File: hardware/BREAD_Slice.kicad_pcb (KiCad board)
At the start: 2 copper layers, 70 x 100 mm, 22 parts, among them J1 Conn_01x10_Socket, SW1 SW_DIP_x04, U1 AP63205

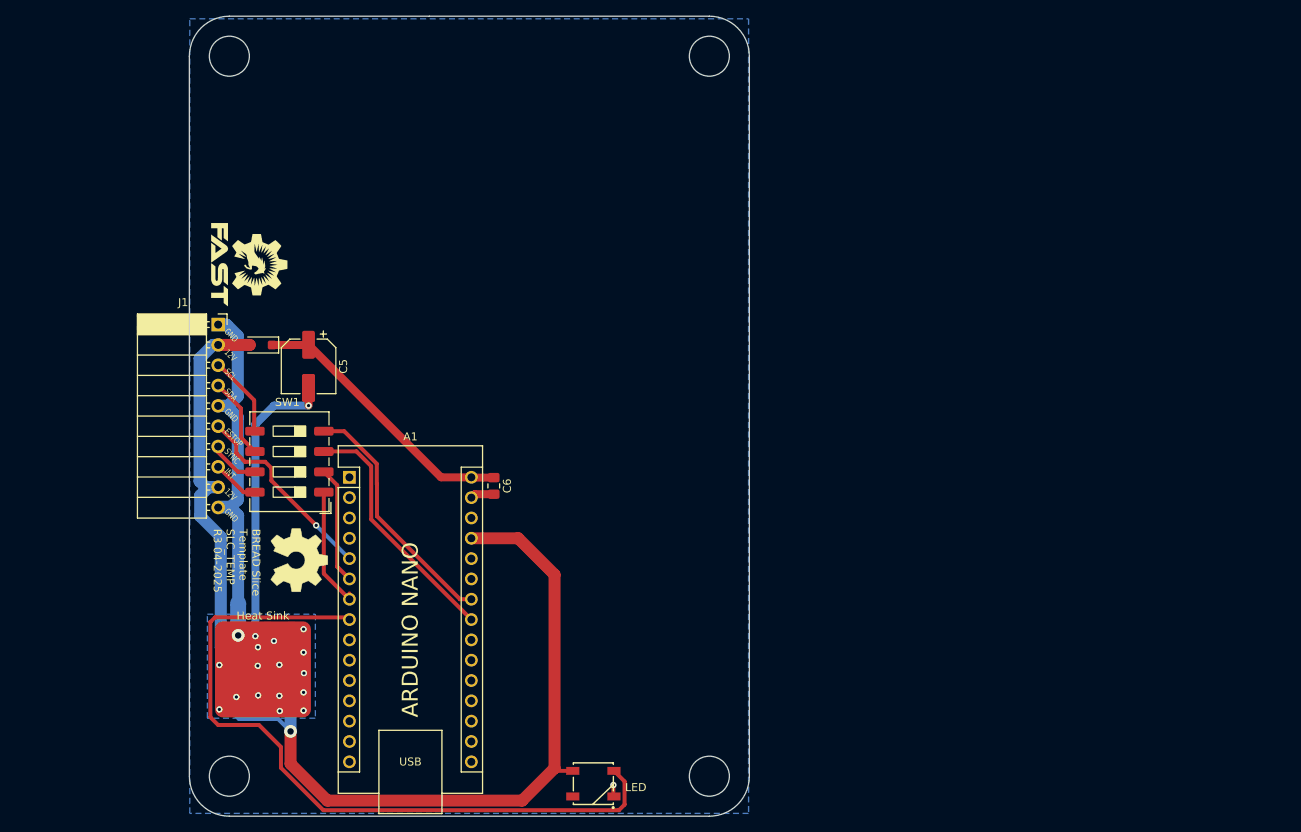
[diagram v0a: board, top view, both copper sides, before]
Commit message: added level shifter and started layout
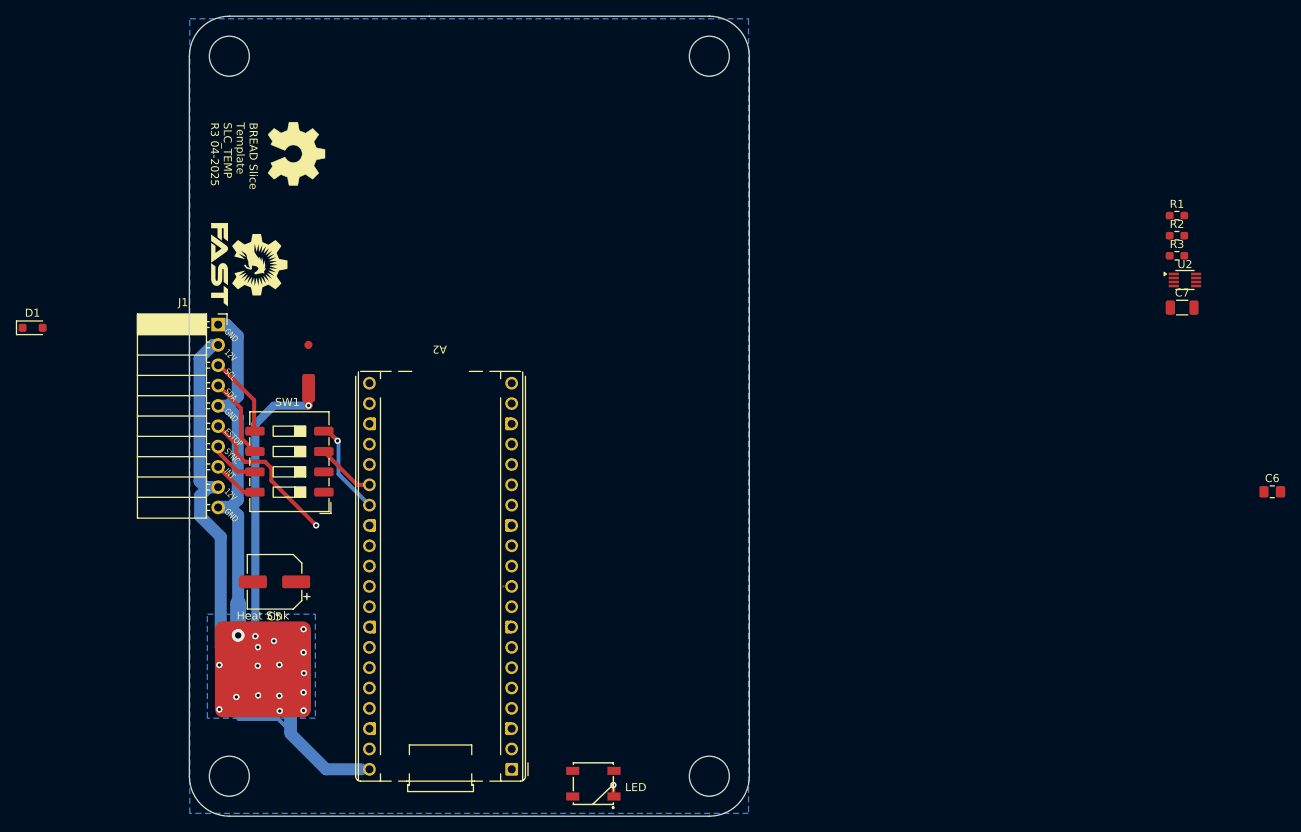
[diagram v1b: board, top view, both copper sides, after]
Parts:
- removed A1: Arduino_Nano_v3.x, KMLib_Boards_Modules:Arduino_Nano_Headers
- added A2: RaspberryPi_Pico, KMLib_Boards_Modules:RaspberryPi_Pico_THT, F.Cu at (162.9, 133.9)
- added C7: 100nF, Capacitor_SMD:C_1206_3216Metric, F.Cu at (246.7, 76.2)
- added R1: 4.7k, Resistor_SMD:R_0603_1608Metric_Pad0.98x0.95mm_HandSolder, F.Cu at (246.1, 64.7)
- added R2: 4.7k, Resistor_SMD:R_0603_1608Metric_Pad0.98x0.95mm_HandSolder, F.Cu at (246.1, 67.2)
- added R3: 200k, Resistor_SMD:R_0603_1608Metric_Pad0.98x0.95mm_HandSolder, F.Cu at (246.1, 69.7)
- added U2: PCA9306DC1, Package_SO:VSSOP-8_2.3x2mm_P0.5mm, F.Cu at (247.1, 72.8)
- D1: value 1N4007 -> BAT54WS-7-F; footprint Diode_SMD:D_SOD-123F -> Diode_SMD:D_SOD-323_HandSoldering
- moved C6 97.3 mm to (258.0, 99.2), turned to 0 degrees
- moved Ref** 50.8 mm to (135.6, 57.0)
- moved D1 28.6 mm to (103.0, 78.8), turned to 0 degrees
- moved C5 27.3 mm to (133.2, 110.5), turned to 180 degrees
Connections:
- net /slice_template/VIN renamed /slice_template/VSYS
- D1 pad 2: +12V -> +5V
- SW1 pad 3: /slice_template/I2C_DAT/A4 -> /slice_template/I2C0_SDA/GPIO20
- SW1 pad 4: /slice_template/I2C_CLK/A5 -> /slice_template/I2C0_CLK/GPIO21
- SW1 pad 5: /slice_template/I2C_CLK -> Net-(U2-SCL1)
- SW1 pad 6: /slice_template/I2C_DAT -> Net-(U2-SDA1)
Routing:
- net /slice_template/LED: track 92.9 -> 0.00 mm
- net +5V: track 104.2 -> 37.4 mm, vias 1 -> 0
- net /slice_template/VSYS: track 34.6 -> 0.04 mm
- net /slice_template/I2C_DAT/A4: track 31.1 -> 0.00 mm
- net /slice_template/I2C_CLK/A5: track 31.0 -> 0.00 mm
- net /slice_template/INT/CAN_{CS}: track 15.4 -> 0.00 mm
- net /slice_template/SYNC/CAN_{INT}: track 14.9 -> 0.00 mm
- net /slice_template/I2C0_CLK/GPIO21: track 0.00 -> 11.9 mm, vias 0 -> 1
- net /slice_template/I2C0_SDA/GPIO20: track 0.00 -> 7.42 mm
- net /slice_template/ESTOP: track 25.9 -> 19.6 mm
- net +12V: track 52.1 -> 48.2 mm
- net GND: track 57.3 -> 54.3 mm
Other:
- board text removed: "ARDUINO NANO"

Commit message: finished layout
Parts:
- removed C7: 100nF, Capacitor_SMD:C_1206_3216Metric
- removed R1, R2: 4.7k, Resistor_SMD:R_0603_1608Metric_Pad0.98x0.95mm_HandSolder
- removed R3: 200k, Resistor_SMD:R_0603_1608Metric_Pad0.98x0.95mm_HandSolder
- removed U2: PCA9306DC1, Package_SO:VSSOP-8_2.3x2mm_P0.5mm
- moved C6 122.5 mm to (140.5, 134.0), turned to -90 degrees
- moved D1 56.1 mm to (140.5, 120.5), turned to 90 degrees
- moved C5 17.2 mm to (138.0, 127.0), turned to -90 degrees
- moved C4 6.76 mm to (133.8, 109.6)
- moved NT1 6.76 mm to (128.7, 108.4)
- moved C1 6.75 mm to (128.8, 112.7)
- moved C2 6.75 mm to (131.2, 119.5)
- moved C3 6.75 mm to (133.8, 112.7)
- moved L1 6.75 mm to (133.8, 116.0)
- moved U1 6.75 mm to (128.8, 116.0)
- moved HS1 6.45 mm to (131.8, 115.0)
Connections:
- net /slice_template/SPI0_MISO/GPIO16 renamed /slice_template/GPIO16
- net /slice_template/SPI0_MOSI/GPIO19 renamed /slice_template/GPIO19
- net /slice_template/SPI0_SCK/GPIO18 renamed /slice_template/GPIO18
- net /slice_template/SPI0_~{CS}/GPIO17 renamed /slice_template/GPIO17
- A2 pad 2: /slice_template/SYNC/CAN_{INT} -> /slice_template/LED
- A2 pad 29: /slice_template/GPIO22 -> /slice_template/SYNC/CAN_{INT}
- A2 pad 31: /slice_template/GPIO26_ADC0 -> /slice_template/INT/CAN_{CS}
- A2 pad 4: /slice_template/INT/CAN_{CS} -> unconnected-(A2-GPIO2-Pad4)
- A2 pad 5: /slice_template/LED -> unconnected-(A2-GPIO3-Pad5)
- SW1 pad 5: Net-(U2-SCL1) -> /slice_template/I2C_CLK
- SW1 pad 6: Net-(U2-SDA1) -> /slice_template/I2C_DAT
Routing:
- net /slice_template/ESTOP: track 19.6 -> 93.9 mm, vias 1 -> 0
- net +5V: track 37.4 -> 87.3 mm, vias 0 -> 3
- net /slice_template/VSYS: track 0.04 -> 19.3 mm
- net /slice_template/INT/CAN_{CS}: track 0.00 -> 14.1 mm
- net /slice_template/LED: track 0.00 -> 13.9 mm
- net /slice_template/SYNC/CAN_{INT}: track 0.00 -> 12.3 mm
- net GND: track 54.3 -> 47.6 mm
- net GNDPWR: track 43.7 -> 36.9 mm
- net +12V: track 48.2 -> 41.4 mm

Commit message: pcb: minor changes and silk screen version
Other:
- board text added: "BREAD Slice Template SLC_TEMP R0 03-2026"
- board text removed: "BREAD Slice Template SLC_TEMP R3 04-2025"
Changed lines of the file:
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@@
 		)
 	)
-	(gr_text "BREAD Slice\nTemplate\nSLC_TEMP\nR3 04-2025"
+	(gr_text "BREAD Slice\nTemplate\nSLC_TEMP\nR0 03-2026"
 		(at 128.175 53.075 270)
 		(layer "F.SilkS")

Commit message: chore: change version to v1 to align with template name
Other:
- board text added: "BREAD Slice Template SLC_TEMP R1 03-2026"
- board text removed: "BREAD Slice Template SLC_TEMP R0 03-2026"
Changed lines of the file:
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@@
 		)
 	)
-	(gr_text "BREAD Slice\nTemplate\nSLC_TEMP\nR0 03-2026"
+	(gr_text "BREAD Slice\nTemplate\nSLC_TEMP\nR1 03-2026"
 		(at 128.175 53.075 270)
 		(layer "F.SilkS")

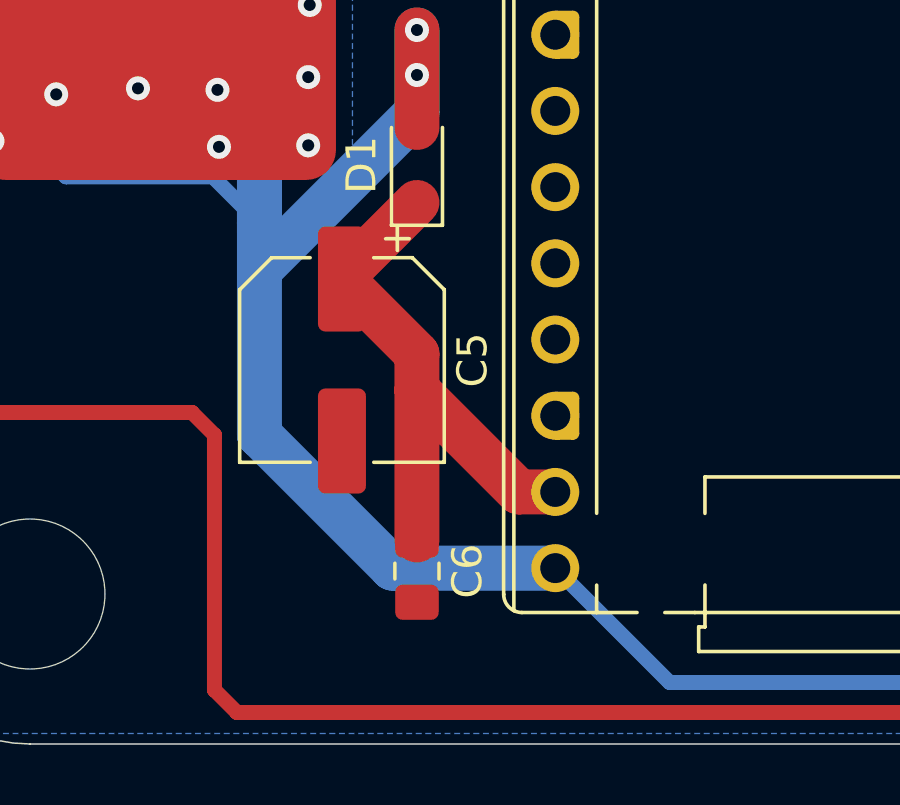
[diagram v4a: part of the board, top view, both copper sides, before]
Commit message: fix: rewire gnd caps around pico
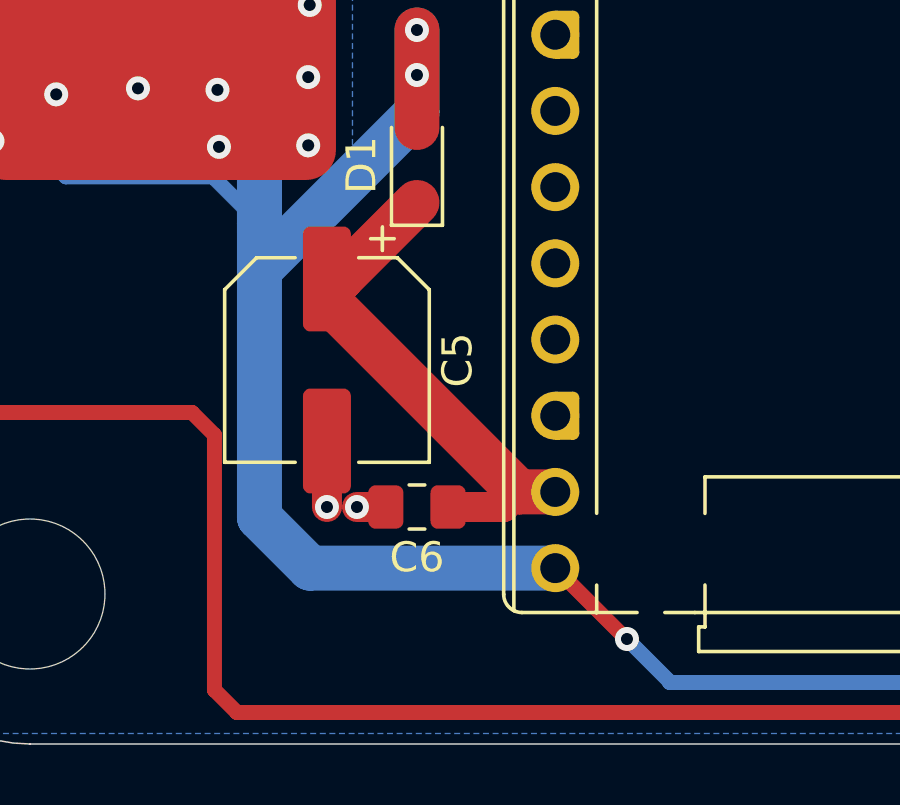
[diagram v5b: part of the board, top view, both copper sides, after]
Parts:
- moved C6 2.14 mm to (140.5, 131.9), turned to 180 degrees
- moved C5 0.50 mm to (137.5, 127.0)
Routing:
- net GND: track 47.6 -> 50.7 mm, vias 19 -> 21
- net /slice_template/VSYS: track 19.3 -> 17.6 mm
- net +5V: track 87.3 -> 89.0 mm, vias 3 -> 4
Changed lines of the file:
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@@
 	(footprint "Capacitor_SMD:C_0805_2012Metric_Pad1.18x1.45mm_HandSolder"
 		(layer "F.Cu")
-		(at 140.5 134.0375 -90)
+		(at 140.5 131.9 180)
 		(descr "Capacitor SMD 0805 (2012 Metric), square (rectangular) end terminal, IPC-7351 nominal with elongated pad for handsoldering. (Body size source: IPC-SM-782 page 76, https://www.pcb-3d.com/wordpress/wp-content/uploads/ipc-sm-782a_amendment_1_and_2.pdf, https://docs.google.com/spreadsheets/d/1BsfQQcO9C6DZCsRaXUlFlo91Tg2WpOkGARC1WS5S8t0/edit?usp=sharing), generated with kicad-footprint-generator")
 		(tags "capacitor handsolder")
 		(property "Reference" "C6"
-			(at 0 -1.68 90)
+			(at 0 -1.68 0)
 			(layer "F.SilkS")
 			(effects
@@
 		)
 		(property "Value" "0.1u"
-			(at 0 1.68 90)
+			(at 0 1.68 0)
 			(layer "F.Fab")
 			(effects
@@
 		)
 		(property "Datasheet" "~"
-			(at 0 0 90)
+			(at 0 0 0)
 			(layer "F.Fab")
 			(hide yes)
@@
 		)
 		(property "Description" "Unpolarized capacitor"
-			(at 0 0 90)
+			(at 0 0 0)
 			(layer "F.Fab")
 			(hide yes)
@@
 		)
 		(fp_line
-			(start -1.88 0.98)
-			(end -1.88 -0.98)
+			(start 1.88 0.98)
+			(end -1.88 0.98)
 			(stroke
 				(width 0.05)
@@
 		)
 		(fp_line
-			(start 1.88 0.98)
-			(end -1.88 0.98)
+			(start 1.88 -0.98)
+			(end 1.88 0.98)
 			(stroke
 				(width 0.05)
@@
 		)
 		(fp_line
-			(start -1.88 -0.98)
-			(end 1.88 -0.98)
+			(start -1.88 0.98)
+			(end -1.88 -0.98)
 			(stroke
 				(width 0.05)
@@
 		)
 		(fp_line
-			(start 1.88 -0.98)
-			(end 1.88 0.98)
+			(start -1.88 -0.98)
+			(end 1.88 -0.98)
 			(stroke
 				(width 0.05)
@@
 		)
 		(fp_line
-			(start -1 0.625)
-			(end -1 -0.625)
+			(start 1 0.625)
+			(end -1 0.625)
 			(stroke
 				(width 0.1)
@@
 		)
 		(fp_line
-			(start 1 0.625)
-			(end -1 0.625)
+			(start 1 -0.625)
+			(end 1 0.625)
 			(stroke
 				(width 0.1)
@@
 		)
 		(fp_line
-			(start -1 -0.625)
-			(end 1 -0.625)
+			(start -1 0.625)
+			(end -1 -0.625)
 			(stroke
 				(width 0.1)
@@
 		)
 		(fp_line
-			(start 1 -0.625)
-			(end 1 0.625)
+			(start -1 -0.625)
+			(end 1 -0.625)
 			(stroke
 				(width 0.1)
@@
 		)
 		(fp_text user "${REFERENCE}"
-			(at 0 0 90)
+			(at 0 0 0)
 			(layer "F.Fab")
 			(effects
@@
 		)
 		(pad "1" smd roundrect
-			(at -1.0375 0 270)
+			(at -1.0375 0 180)
 			(size 1.175 1.45)
 			(layers "F.Cu" "F.Mask" "F.Paste")
@@
 		)
 		(pad "2" smd roundrect
-			(at 1.0375 0 270)
+			(at 1.0375 0 180)
 			(size 1.175 1.45)
 			(layers "F.Cu" "F.Mask" "F.Paste")
@@
 	(footprint "Capacitor_SMD:CP_Elec_6.3x7.7"
 		(layer "F.Cu")
-		(at 138 127 -90)
+		(at 137.5 127 -90)
 		(descr "SMD capacitor, aluminum electrolytic, Nichicon, 6.3x7.7mm")
 		(tags "capacitor electrolytic")
@@
 	)
 	(segment
+		(start 139.4625 131.9)
+		(end 138.5 131.9)
+		(width 1)
+		(layer "F.Cu")
+		(net 3)
+	)
+	(segment
 		(start 137.5 86.275)
 		(end 137.5 88.475)
@@
 		(net 3)
 	)
+	(segment
+		(start 137.5 129.7)
+		(end 137.5 131.9)
+		(width 1)
+		(layer "F.Cu")
+		(net 3)
+	)
 	(via
 		(at 133.85 114.12)
@@
 	)
 	(via
+		(at 137.5 131.9)
+		(size 0.8)
+		(drill 0.4)
+		(layers "F.Cu" "B.Cu")
+		(net 3)
+	)
+	(via
 		(at 133.85 117.995)
 		(size 0.8)
@@
 		(net 3)
 	)
+	(via
+		(at 138.5 131.9)
+		(size 0.8)
+		(drill 0.4)
+		(layers "F.Cu" "B.Cu")
+		(net 3)
+	)
 	(segment
 		(start 128.7 110.445)
@@
 	)
 	(segment
+		(start 147.5 136.3)
+		(end 147.4725 136.3)
+		(width 0.5)
+		(layer "F.Cu")
+		(net 5)
+	)
+	(segment
 		(start 170.532769 134.132769)
 		(end 170.523 134.132769)
@@
 		(net 5)
 	)
+	(segment
+		(start 147.4725 136.3)
+		(end 145.11 133.9375)
+		(width 0.5)
+		(layer "F.Cu")
+		(net 5)
+	)
 	(via
 		(at 140.5 117.5)
@@
 		(net 5)
 	)
-	(segment
-		(start 139.6875 133.9375)
-		(end 145.11 133.9375)
-		(width 1.5)
-		(layer "B.Cu")
-		(net 5)
-	)
-	(segment
-		(start 135.25 124)
-		(end 135.25 129.5)
-		(width 1.5)
-		(layer "B.Cu")
+	(via
+		(at 147.5 136.3)
+		(size 0.8)
+		(drill 0.4)
+		(layers "F.Cu" "B.Cu")
 		(net 5)
 	)
 	(segment
-		(start 148.9225 137.75)
+		(start 136.9375 133.9375)
 		(end 145.11 133.9375)
-		(width 0.5)
+		(width 1.5)
 		(layer "B.Cu")
 		(net 5)
@@
 	)
 	(segment
+		(start 135.25 132.25)
+		(end 136.9375 133.9375)
+		(width 1.5)
+		(layer "B.Cu")
+		(net 5)
+	)
+	(segment
 		(start 140.5 118.75)
 		(end 140.5 116)
@@
 	)
 	(segment
+		(start 148.9225 137.75)
+		(end 148.9225 137.7225)
+		(width 0.5)
+		(layer "B.Cu")
+		(net 5)
+	)
+	(segment
 		(start 135.3 112.725)
 		(end 135.3 115.95)
@@
 	)
 	(segment
+		(start 148.9225 137.7225)
+		(end 147.5 136.3)
+		(width 0.5)
+		(layer "B.Cu")
+		(net 5)
+	)
+	(segment
+		(start 135.25 124)
+		(end 135.25 132.25)
+		(width 1.5)
+		(layer "B.Cu")
+		(net 5)
+	)
+	(segment
 		(start 135.325 115.925)
 		(end 135.25 116)
@@
 	)
 	(segment
-		(start 135.25 129.5)
-		(end 139.6875 133.9375)
-		(width 1.5)
-		(layer "B.Cu")
-		(net 5)
-	)
-	(segment
 		(start 135.3 115.95)
 		(end 135.25 116)
@@
 	)
 	(segment
-		(start 138 124.25)
-		(end 140.5 121.75)
-		(width 1.5)
+		(start 143.395 131.9)
+		(end 143.8975 131.3975)
+		(width 1)
 		(layer "F.Cu")
 		(net 22)
 	)
 	(segment
-		(start 140.5 126.8)
-		(end 138 124.3)
+		(start 145.11 131.3975)
+		(end 143.8975 131.3975)
 		(width 1.5)
 		(layer "F.Cu")
@@
 	(segment
 		(start 143.8975 131.3975)
-		(end 140.5 128)
+		(end 137.5 125)
 		(width 1.5)
 		(layer "F.Cu")
@@
 	)
 	(segment
-		(start 145.11 131.3975)
-		(end 143.8975 131.3975)
+		(start 137.95 124.3)
+		(end 140.5 121.75)
 		(width 1.5)
 		(layer "F.Cu")
@@
 	)
 	(segment
-		(start 138 124.3)
-		(end 138 124.25)
-		(width 1.5)
+		(start 141.5375 131.9)
+		(end 143.395 131.9)
+		(width 1)
 		(layer "F.Cu")
 		(net 22)
 	)
 	(segment
-		(start 140.5 133)
-		(end 140.5 128)
+		(start 137.5 124.3)
+		(end 137.95 124.3)
 		(width 1.5)
 		(layer "F.Cu")
@@
 	)
 	(segment
-		(start 140.5 128)
-		(end 140.5 126.8)
+		(start 137.5 125)
+		(end 137.5 124.3)
 		(width 1.5)
 		(layer "F.Cu")
